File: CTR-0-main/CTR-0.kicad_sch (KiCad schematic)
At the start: 38 parts, among them J1 USB_C_Receptacle_USB2.0_14P, J2 Conn_01x20, J3 Conn_01x20, J4 Conn_01x03, SW1 SW_Push, SW2 SW_Push, U1 RP2040, U2 NCP1117-3.3_SOT223, U3 W25Q128JVS, U4 TVS1400DRV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

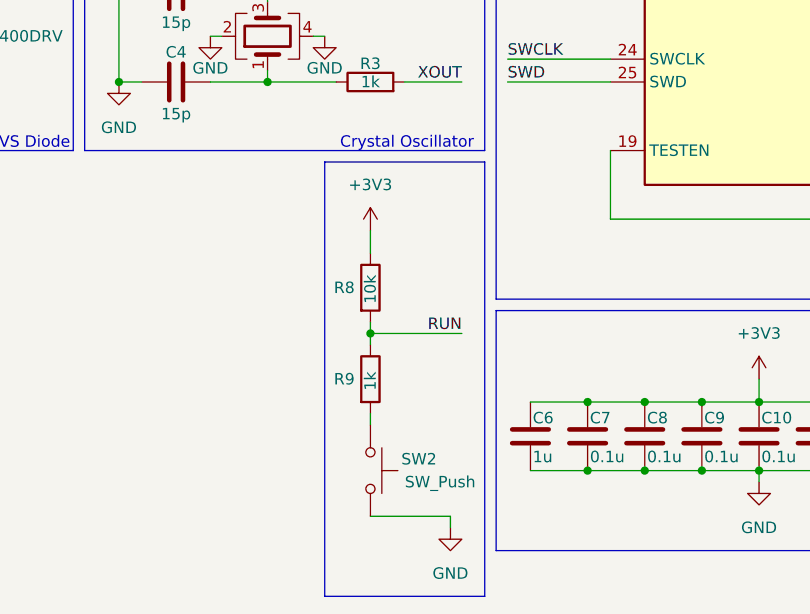
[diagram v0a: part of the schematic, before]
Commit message: Add files via upload
fixed drc gnd net
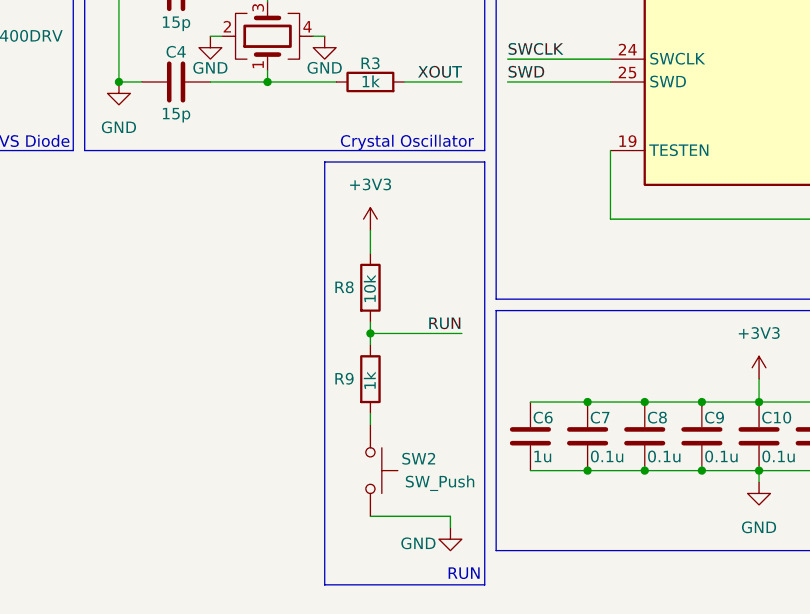
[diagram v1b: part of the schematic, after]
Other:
- note added: "RUN"
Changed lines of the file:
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@@
 	(rectangle
 		(start 115.57 107.95)
-		(end 133.35 156.21)
+		(end 133.35 154.94)
 		(stroke
 			(width 0)
@@
 		)
 	)
+	(text "RUN\n"
+		(exclude_from_sim no)
+		(at 131.064 153.924 0)
+		(effects
+			(font
+				(size 1.27 1.27)
+			)
+		)
+	)
 	(text "TVS Diode\n"
 		(exclude_from_sim no)
@@
 		(on_board yes)
 		(dnp no)
-		(fields_autoplaced yes)
 		(property "Reference" "#PWR022"
 			(at 129.54 154.94 0)
@@
 		)
 		(property "Value" "GND"
-			(at 129.54 153.67 0)
+			(at 125.984 150.368 0)
 			(effects
 				(font
